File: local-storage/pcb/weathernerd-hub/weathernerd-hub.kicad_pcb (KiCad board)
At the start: 2 copper layers, 1 part

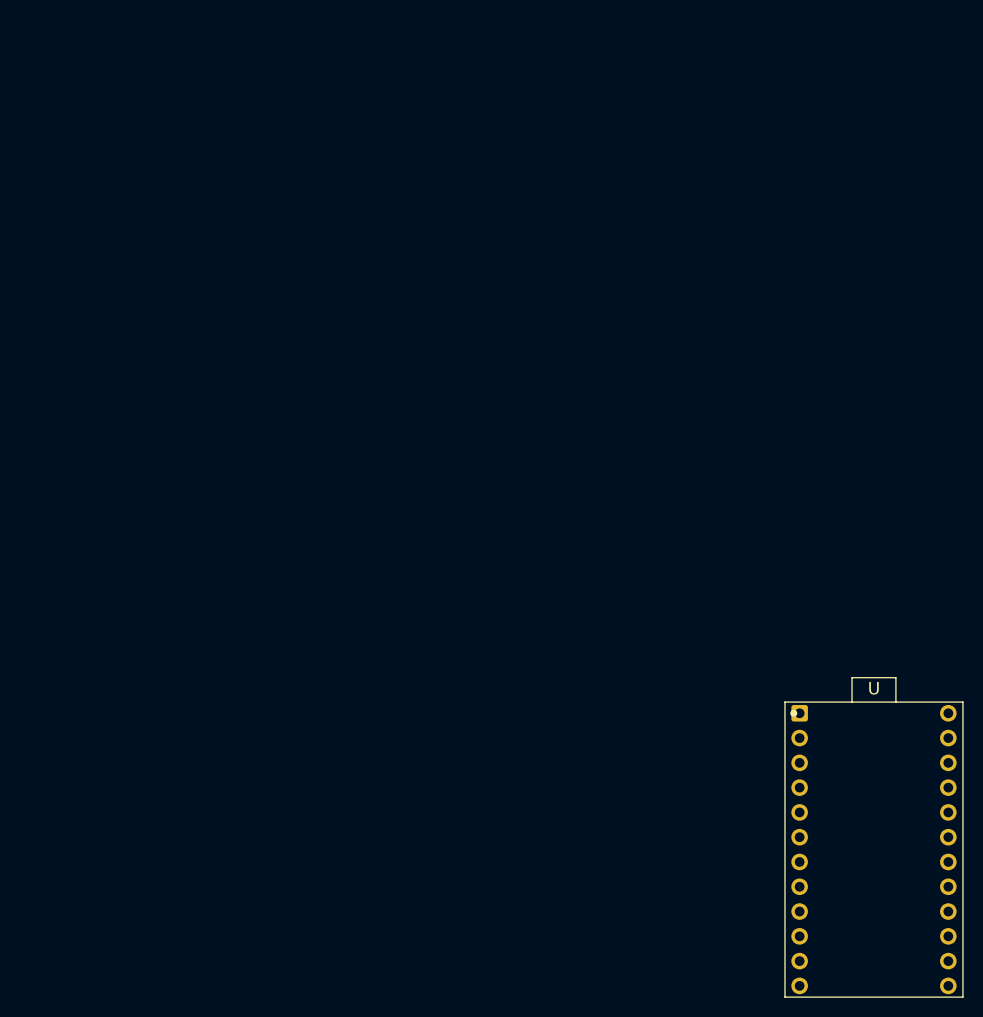
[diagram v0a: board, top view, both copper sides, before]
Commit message: some schematic progress
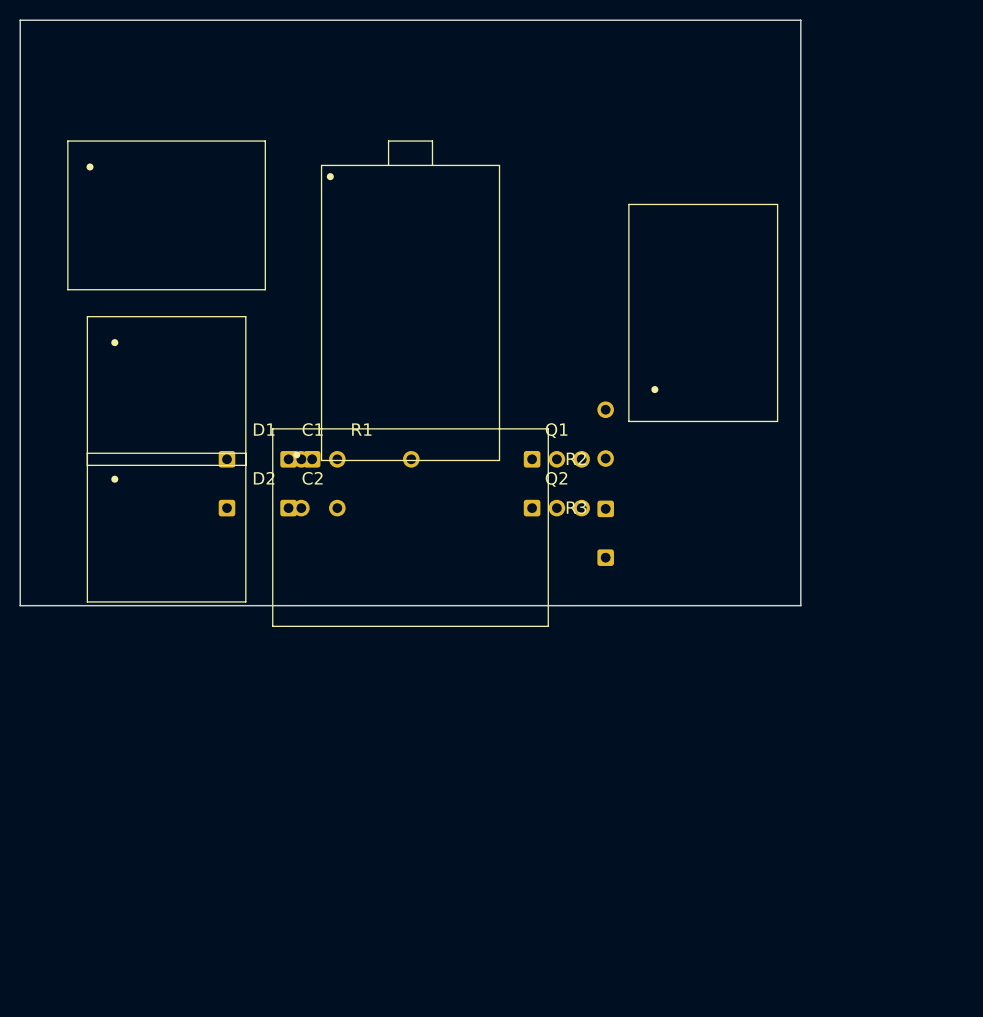
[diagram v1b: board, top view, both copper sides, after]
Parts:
- removed U: ESP32-C6-SuperMini, weathernerd:ESP32-C6-SuperMini
- added ?: , weathernerd:ESP32-C6-SuperMini, F.Cu at (40.0, 30.0)
- added ?: , weathernerd:MicroSD-SPI, F.Cu at (70.0, 30.0)
- added ?: , weathernerd:BME280, F.Cu at (15.0, 20.0)
- added ?: , weathernerd:DS3231, F.Cu at (15.0, 38.0)
- added ?: , weathernerd:OLED-Encoder-Btns, F.Cu at (40.0, 52.0)
- added ?: , weathernerd:WindNerd-Conn, F.Cu at (15.0, 52.0)
- added C1: 1nF, Symbol:cap, F.Cu at (30.0, 45.0)
- added C2: 470nF, Symbol:cap, F.Cu at (30.0, 50.0)
- added D1: 1N4148, Symbol:diode, F.Cu at (25.0, 45.0)
- added D2: 1N4148, Symbol:diode, F.Cu at (25.0, 50.0)
- added Q1: 2N7002, Symbol:transistor, F.Cu at (55.0, 45.0)
- added Q2: AO3401, Symbol:transistor, F.Cu at (55.0, 50.0)
- added R1: 10k, Symbol:resistor, F.Cu at (35.0, 45.0)
- added R2: 10k, Symbol:resistor, F.Cu at (60.0, 45.0)
- added R3: 10k, Symbol:resistor, F.Cu at (60.0, 50.0)
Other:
- board outline added: 80 x 60 mm
- net class Default added: clearance 0.25, trace_width 0.25, via_dia 0.6, via_drill 0.3

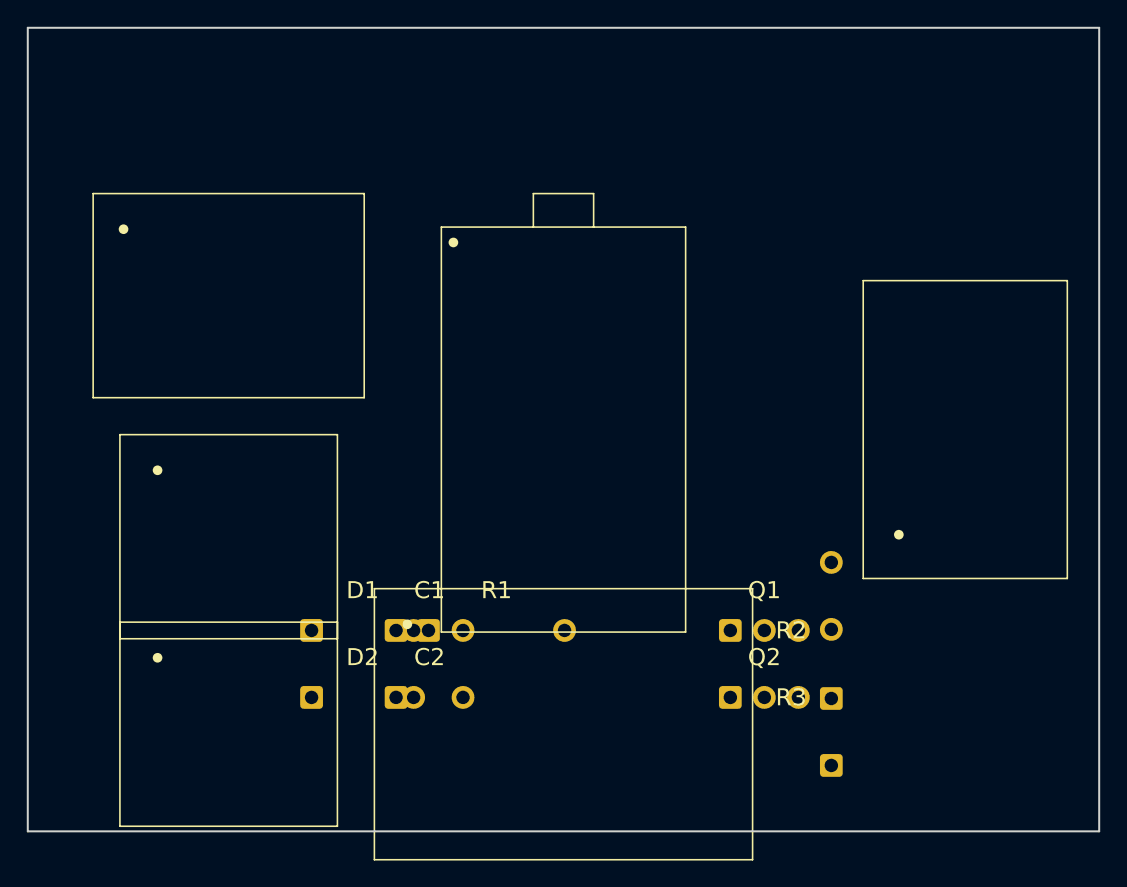
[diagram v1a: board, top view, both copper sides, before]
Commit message: fix pcb starting point
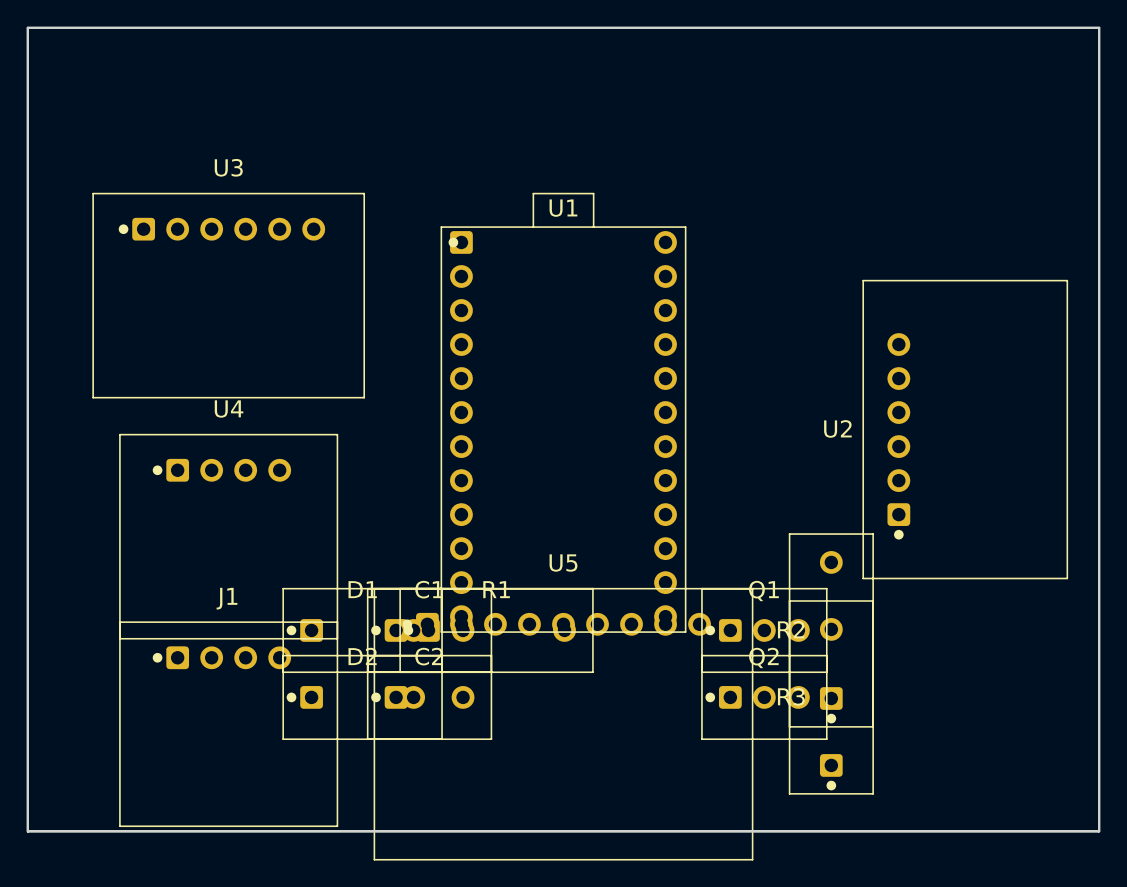
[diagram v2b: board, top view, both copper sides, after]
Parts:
- removed ?: , weathernerd:ESP32-C6-SuperMini
- removed ?: , weathernerd:MicroSD-SPI
- removed ?: , weathernerd:BME280
- removed ?: , weathernerd:DS3231
- removed ?: , weathernerd:OLED-Encoder-Btns
- removed ?: , weathernerd:WindNerd-Conn
- added J1: WindNerd-Conn, WindNerd-Conn, F.Cu at (15.0, 52.0)
- added U1: ESP32-C6-SuperMini, ESP32-C6-SuperMini, F.Cu at (40.0, 30.0)
- added U2: MicroSD-SPI, MicroSD-SPI, F.Cu at (70.0, 30.0)
- added U3: BME280, BME280, F.Cu at (15.0, 20.0)
- added U4: DS3231, DS3231, F.Cu at (15.0, 38.0)
- added U5: OLED-Encoder-Btns, OLED-Encoder-Btns, F.Cu at (40.0, 52.0)
- C1: footprint Symbol:cap -> THT:C1
- C2: footprint Symbol:cap -> THT:C2
- D1: footprint Symbol:diode -> THT:D1
- D2: footprint Symbol:diode -> THT:D2
- Q1: footprint Symbol:transistor -> THT:Q1
- Q2: footprint Symbol:transistor -> THT:Q2
- R1: footprint Symbol:resistor -> THT:R1
- R2: footprint Symbol:resistor -> THT:R2
- R3: footprint Symbol:resistor -> THT:R3

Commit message: the start of a human touch
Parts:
- J1: footprint WindNerd-Conn -> weathernerd:WindNerd-Conn
- R1: footprint THT:R1 -> Resistor_THT:R_Axial_DIN0204_L3.6mm_D1.6mm_P2.54mm_Vertical
- R2: footprint THT:R2 -> Resistor_THT:R_Axial_DIN0204_L3.6mm_D1.6mm_P2.54mm_Vertical
- R3: footprint THT:R3 -> Resistor_THT:R_Axial_DIN0204_L3.6mm_D1.6mm_P2.54mm_Vertical
- moved D1 192.0 mm to (203.8, 115.0)
- moved D2 187.8 mm to (203.8, 107.5)
- moved R1 186.9 mm to (205.1, 122.5)
- moved C1 180.3 mm to (202.5, 97.5)
- moved C2 176.0 mm to (202.5, 85.0)
- moved J1 162.3 mm to (160.0, 125.0)
- moved Q2 138.9 mm to (175.0, 120.0), turned to 90 degrees
- moved Q1 136.5 mm to (175.0, 110.0), turned to 90 degrees
- moved R2 126.5 mm to (175.0, 97.6)
- moved R3 119.8 mm to (170.0, 97.6)
- moved U1 114.7 mm to (139.9, 86.3)
- moved U3 114.1 mm to (115.0, 75.0)
- moved U4 114.0 mm to (113.7, 95.0)
- moved U2 110.7 mm to (170.0, 77.5)
- moved U5 106.4 mm to (117.4, 125.0)
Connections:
- C1 pad 1: (no net) -> Net-(D1-K)
- C1 pad 2: (no net) -> unconnected-(C1-Pad2)
- C2 pad 1: (no net) -> PEAK
- C2 pad 2: (no net) -> GND
- J1 pad GND: (no net) -> GND
- J1 pad RX: (no net) -> WIND_TX
- J1 pad TRG: (no net) -> WIND_TRIG
- J1 pad VCC: (no net) -> +3V3
- Q1 pad D: (no net) -> PEAK
- Q1 pad G: (no net) -> RAIN_RST
- Q1 pad S: (no net) -> GND
- Q2 pad D: (no net) -> OLED_PWR
- Q2 pad G: (no net) -> OLED_GATE
- Q2 pad S: (no net) -> +3V3
- R1 pad 1: (no net) -> PEAK
- R1 pad 2: (no net) -> RAIN_ADC
- R2 pad 1: (no net) -> RAIN_RST
- R2 pad 2: (no net) -> GND
- R3 pad 1: (no net) -> OLED_GATE
- R3 pad 2: (no net) -> +3V3
- U1 pad 0: (no net) -> RAIN_ADC
- U1 pad 1: (no net) -> WIND_TRIG
- U1 pad 12: (no net) -> unconnected-(U1-IO12-Pad12)
- U1 pad 13: (no net) -> unconnected-(U1-IO13-Pad13)
- U1 pad 14: (no net) -> ENC_A
- U1 pad 15: (no net) -> unconnected-(U1-IO15-Pad15)
- U1 pad 16: (no net) -> unconnected-(U1-IO16-Pad16)
- U1 pad 17: (no net) -> unconnected-(U1-IO17-Pad17)
- U1 pad 18: (no net) -> SPI_MOSI
- U1 pad 19: (no net) -> SPI_MISO
- U1 pad 2: (no net) -> SPI_SCK
- U1 pad 20: (no net) -> ENC_B
- U1 pad 22: (no net) -> CON_BTN
- U1 pad 23: (no net) -> BAK_BTN
- U1 pad 3: (no net) -> SPI_CS
- U1 pad 3V3: (no net) -> +3V3
- U1 pad 4: (no net) -> WIND_TX
- U1 pad 5: (no net) -> OLED_GATE
- U1 pad 5V: (no net) -> unconnected-(U1-Pad5V)
- U1 pad 6: (no net) -> I2C_SDA
- U1 pad 7: (no net) -> I2C_SCL
- U1 pad 8: (no net) -> RAIN_RST
- U1 pad 9: (no net) -> unconnected-(U1-IO9-Pad9)
- U1 pad GND: (no net) -> GND
- U2 pad 3V3: (no net) -> +3V3
- U2 pad CLK: (no net) -> unconnected-(U2-PadCLK)
- U2 pad CS: (no net) -> SPI_CS
- U2 pad GND: (no net) -> GND
- U2 pad MISO: (no net) -> SPI_MISO
- U2 pad MOSI: (no net) -> SPI_MOSI
- U3 pad CSB: (no net) -> unconnected-(U3-PadCSB)
- U3 pad GND: (no net) -> GND
- U3 pad SCL: (no net) -> I2C_SCL
- U3 pad SDA: (no net) -> I2C_SDA
- U3 pad SDO: (no net) -> unconnected-(U3-PadSDO)
- U3 pad VCC: (no net) -> +3V3
- U4 pad GND: (no net) -> GND
- U4 pad SCL: (no net) -> I2C_SCL
- U4 pad SDA: (no net) -> I2C_SDA
- U4 pad VCC: (no net) -> +3V3
- U5 pad BAK: (no net) -> BAK_BTN
- U5 pad CON: (no net) -> CON_BTN
- U5 pad GND: (no net) -> GND
- U5 pad PSH: (no net) -> ENC_PSH
- U5 pad SCL: (no net) -> I2C_SCL
- U5 pad SDA: (no net) -> I2C_SDA
- U5 pad TRA: (no net) -> ENC_A
- U5 pad TRB: (no net) -> ENC_B
- U5 pad VCC: (no net) -> OLED_PWR
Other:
- net class Default removed
